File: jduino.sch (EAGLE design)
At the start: 21 parts, among them IC1 LM2936Z-5.0, IC2 ATMEGA48/88/168-PU, J4 6V - 30V in, Q1 16 mHz

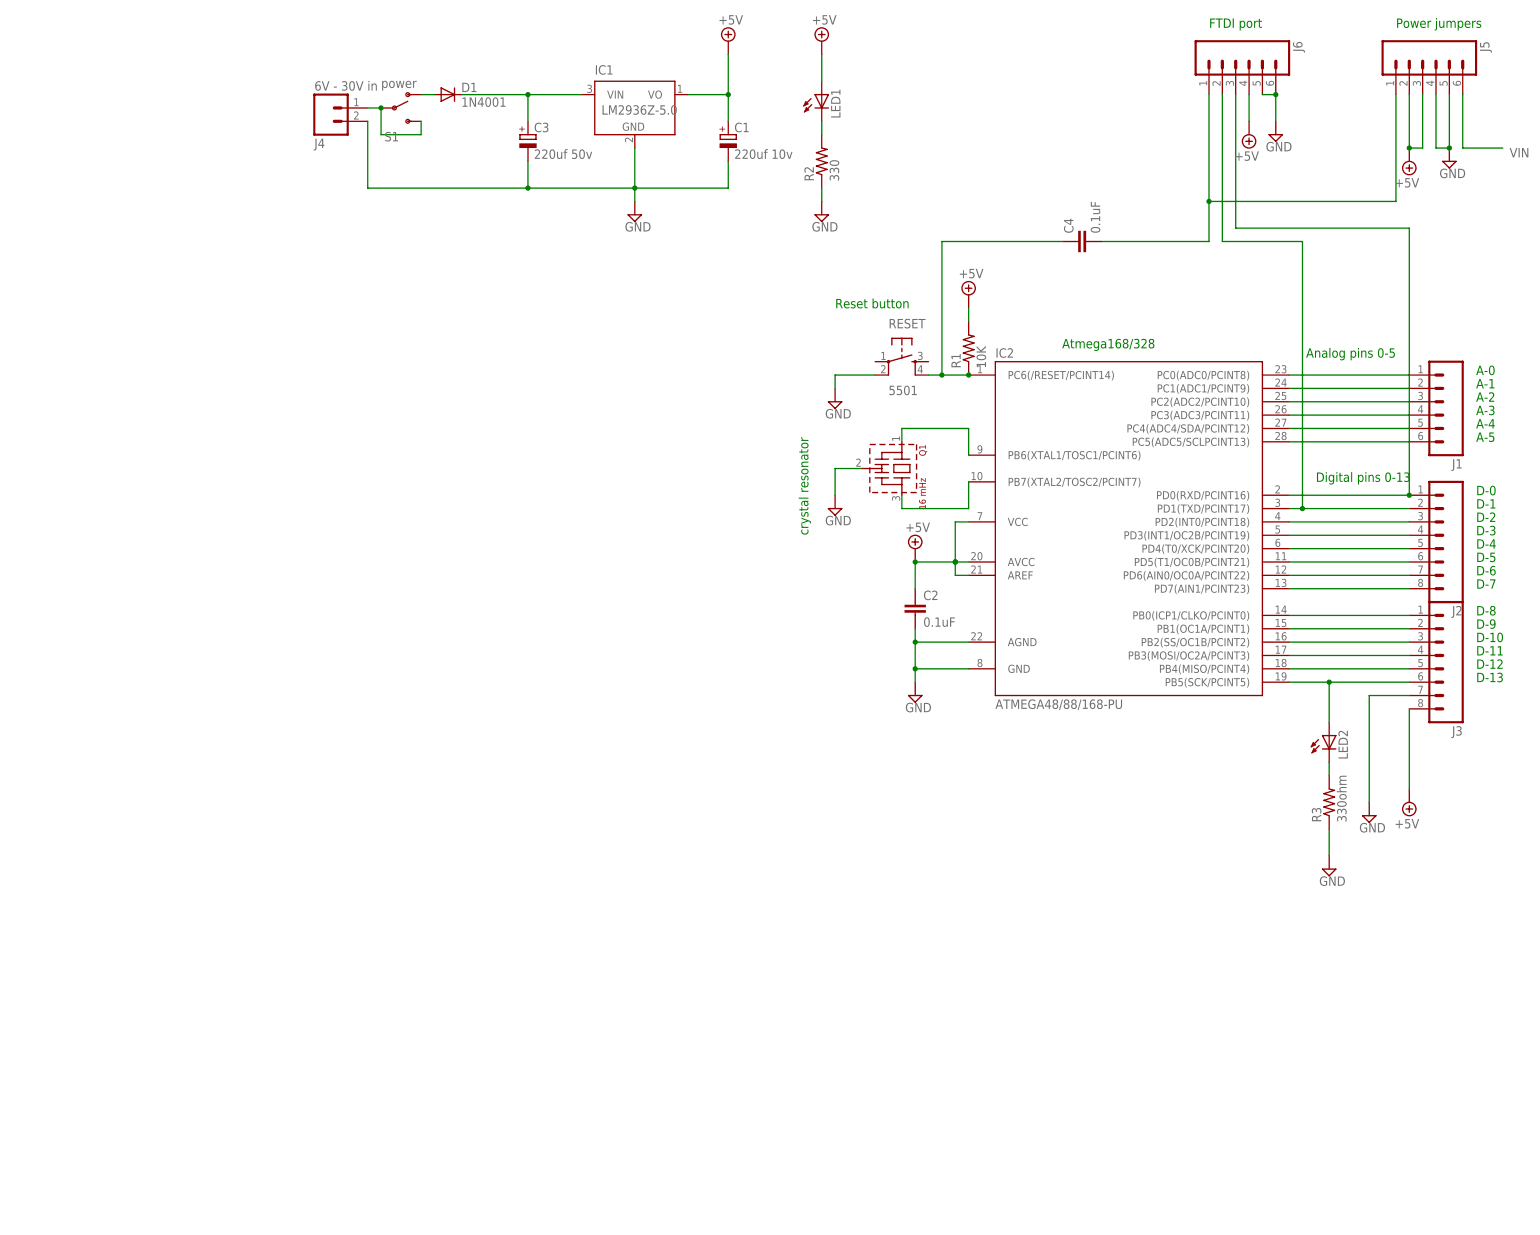
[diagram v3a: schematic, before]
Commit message: Reset adjustments and aesthetic improvements.
Connected reset pin on power jumper before DTR capacitor. Cleaned
up extraneous label and added a frame to the schematic.
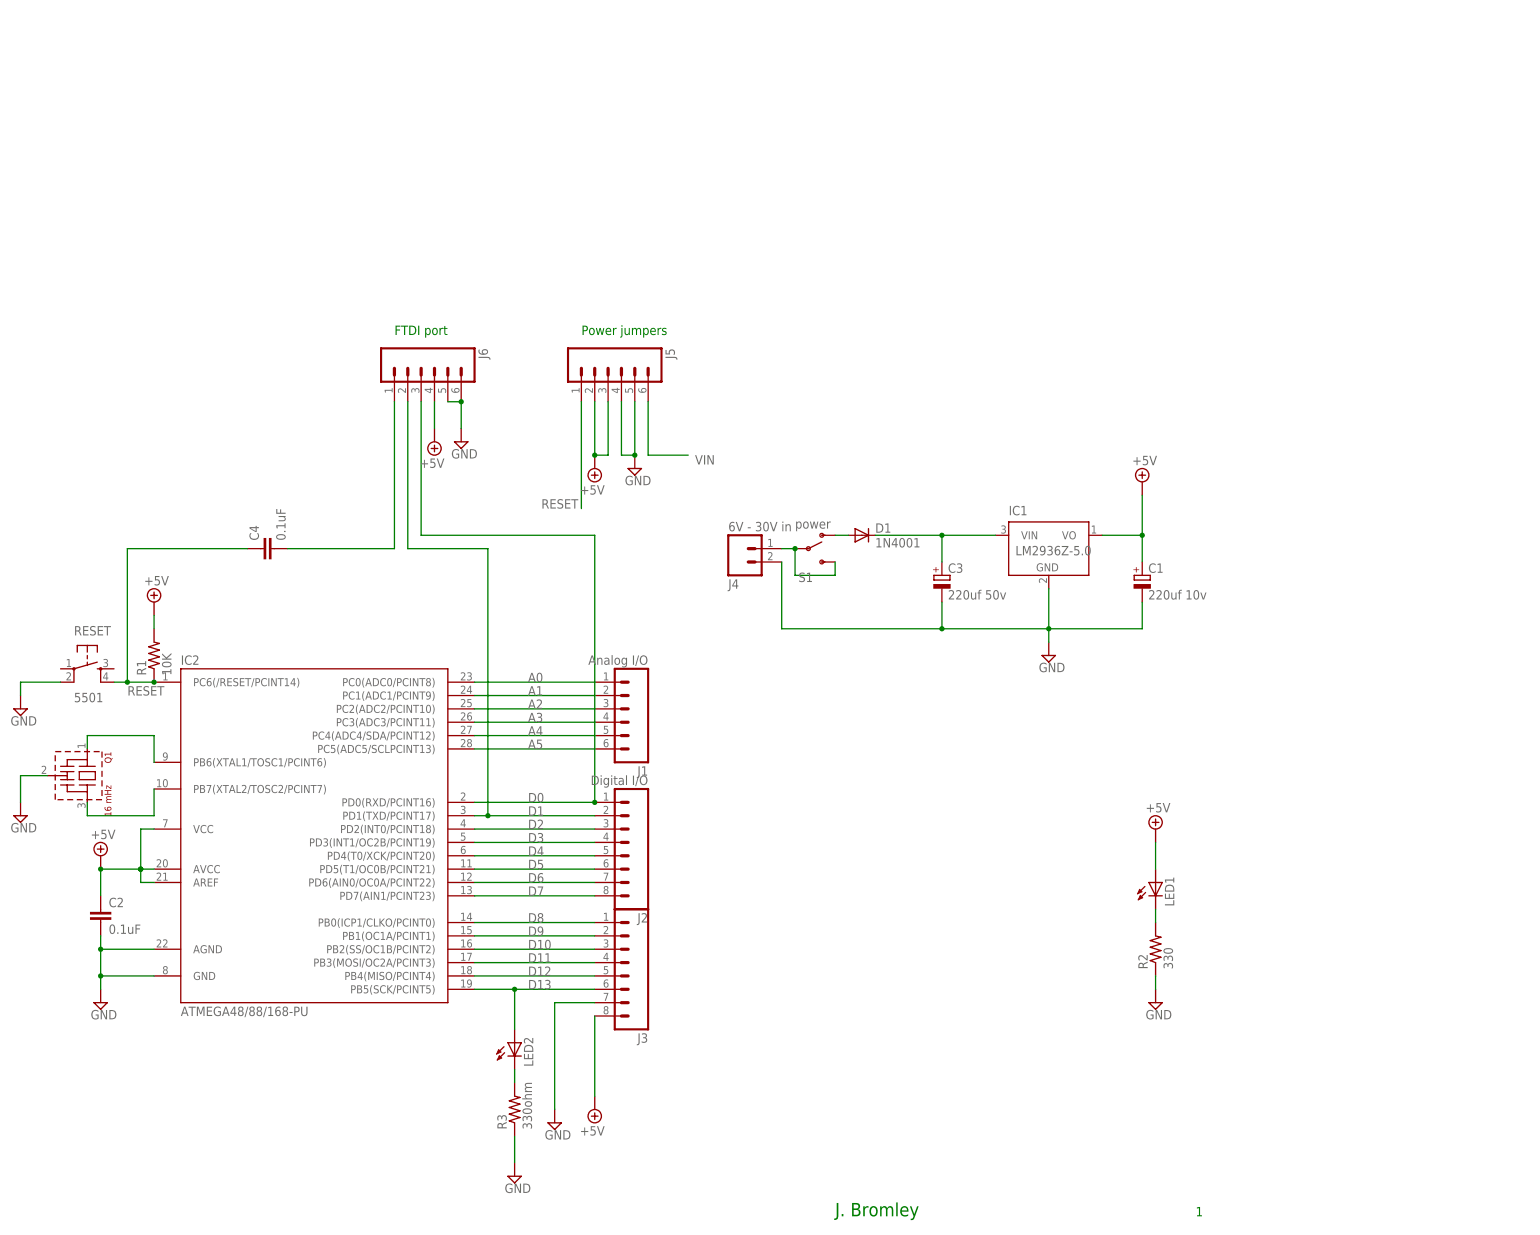
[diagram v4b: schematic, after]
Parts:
- J1: value (none) -> Analog I/O
- J2: value (none) -> Digital I/O
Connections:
- net N$1: no longer J5.1
- net RESET: now also J5.1
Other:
- note added: "1"
- note added: "J. Bromley"
- note removed: "A-0"
- note removed: "A-1"
- note removed: "A-2"
- note removed: "A-3"
- note removed: "A-4"
- note removed: "A-5"
- note removed: "Analog pins 0-5"
- note removed: "Atmega168/328"
- note removed: "D-0"
- note removed: "D-1"
- note removed: "D-10"
- note removed: "D-11"
- note removed: "D-12"
- note removed: "D-13"
- note removed: "D-2"
- note removed: "D-3"
- note removed: "D-4"
- note removed: "D-5"
- note removed: "D-6"
- note removed: "D-7"
- note removed: "D-8"
- note removed: "D-9"
- note removed: "Digital pins 0-13"
- note removed: "Reset button"
- note removed: "crystal resonator"
- moved on the sheet: C1, C2, C3, C4, D1, IC1, IC2, J1, J2, J3, J4, J5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

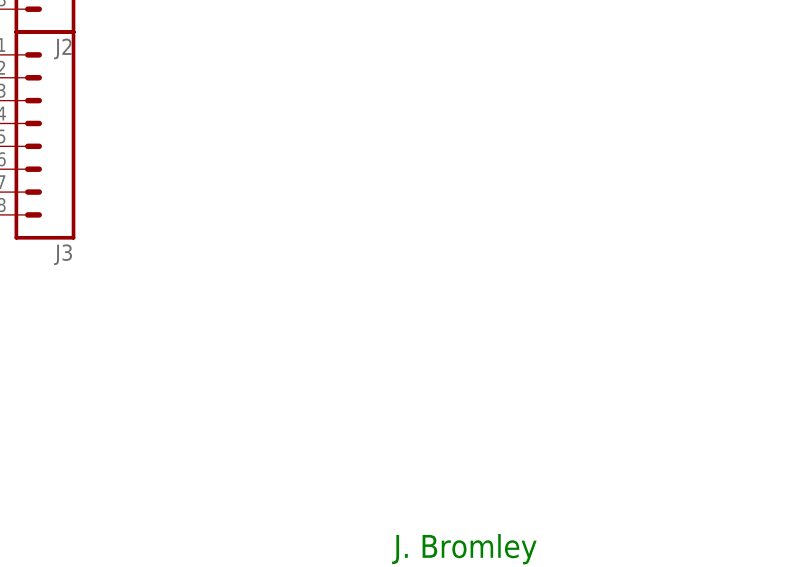
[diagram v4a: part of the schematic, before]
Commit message: Added mounting holes to the board.
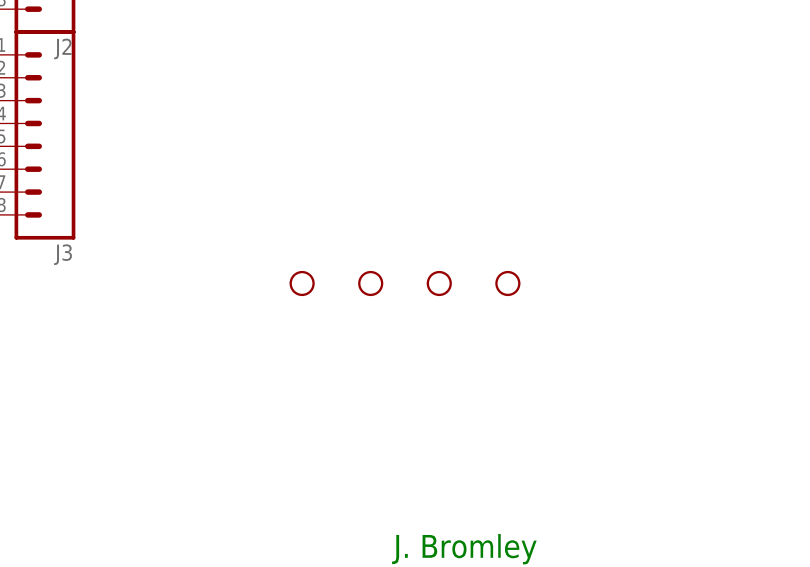
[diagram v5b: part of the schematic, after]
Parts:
- added JP1, JP2, JP3, JP4: STAND-OFF, SparkFun-Electromechanical:STAND-OFF
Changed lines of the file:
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@@
 <?xml version="1.0" encoding="utf-8"?>
 <!DOCTYPE eagle SYSTEM "eagle.dtd">
-<eagle version="6.1">
+<eagle version="6.2">
 <drawing>
 <settings>
@@
 <part name="C4" library="SparkFun-Passives" deviceset="CAP" device="PTH2" value="0.1uF"/>
 <part name="FRAME1" library="SparkFun-Aesthetics" deviceset="FRAME-LETTER" device=""/>
+<part name="JP1" library="SparkFun-Electromechanical" deviceset="STAND-OFF" device=""/>
+<part name="JP2" library="SparkFun-Electromechanical" deviceset="STAND-OFF" device=""/>
+<part name="JP3" library="SparkFun-Electromechanical" deviceset="STAND-OFF" device=""/>
+<part name="JP4" library="SparkFun-Electromechanical" deviceset="STAND-OFF" device=""/>
 </parts>
 <sheets>
@@
 <instance part="FRAME1" gate="G$1" x="-134.62" y="-91.44"/>
 <instance part="FRAME1" gate="G$2" x="12.7" y="-91.44"/>
+<instance part="JP1" gate="G$1" x="27.94" y="-53.34"/>
+<instance part="JP2" gate="G$1" x="35.56" y="-53.34"/>
+<instance part="JP3" gate="G$1" x="43.18" y="-53.34"/>
+<instance part="JP4" gate="G$1" x="50.8" y="-53.34"/>
 </instances>
 <busses>

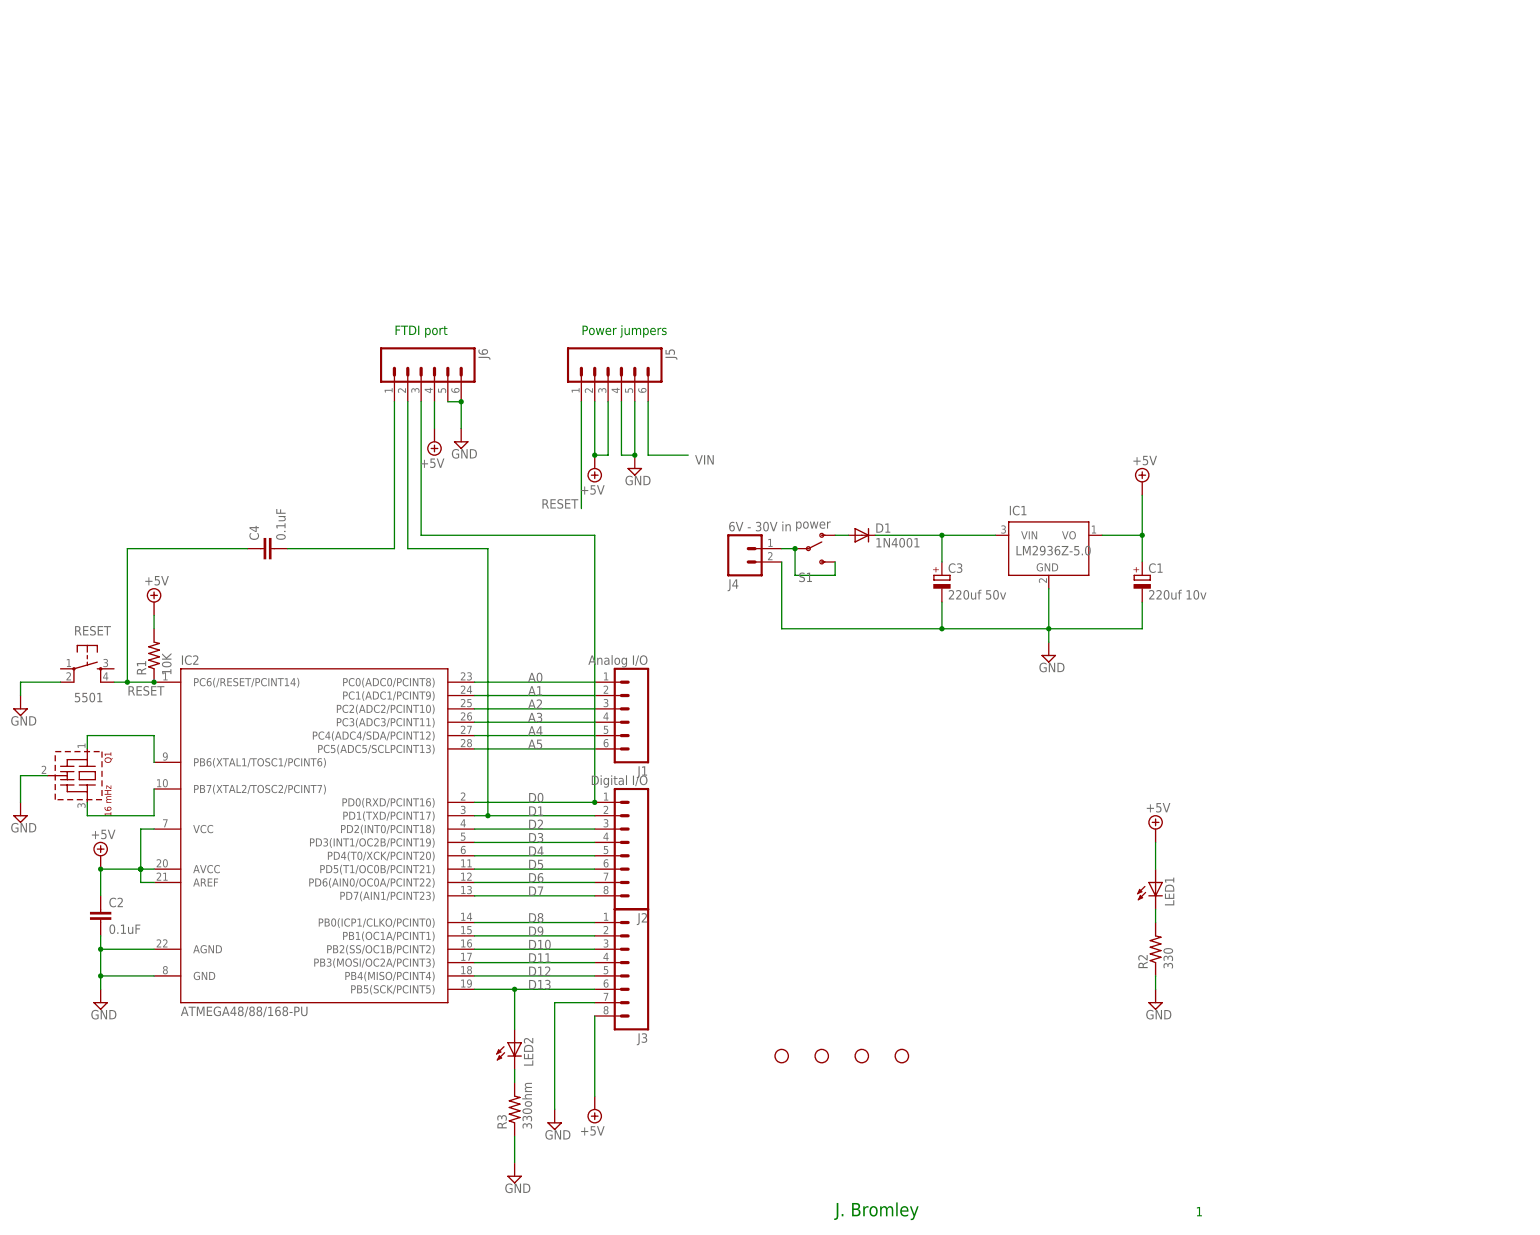
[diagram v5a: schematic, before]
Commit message: Completed layout.
Completed the board layout and sizing. Needed to include four top-side
jumpers.
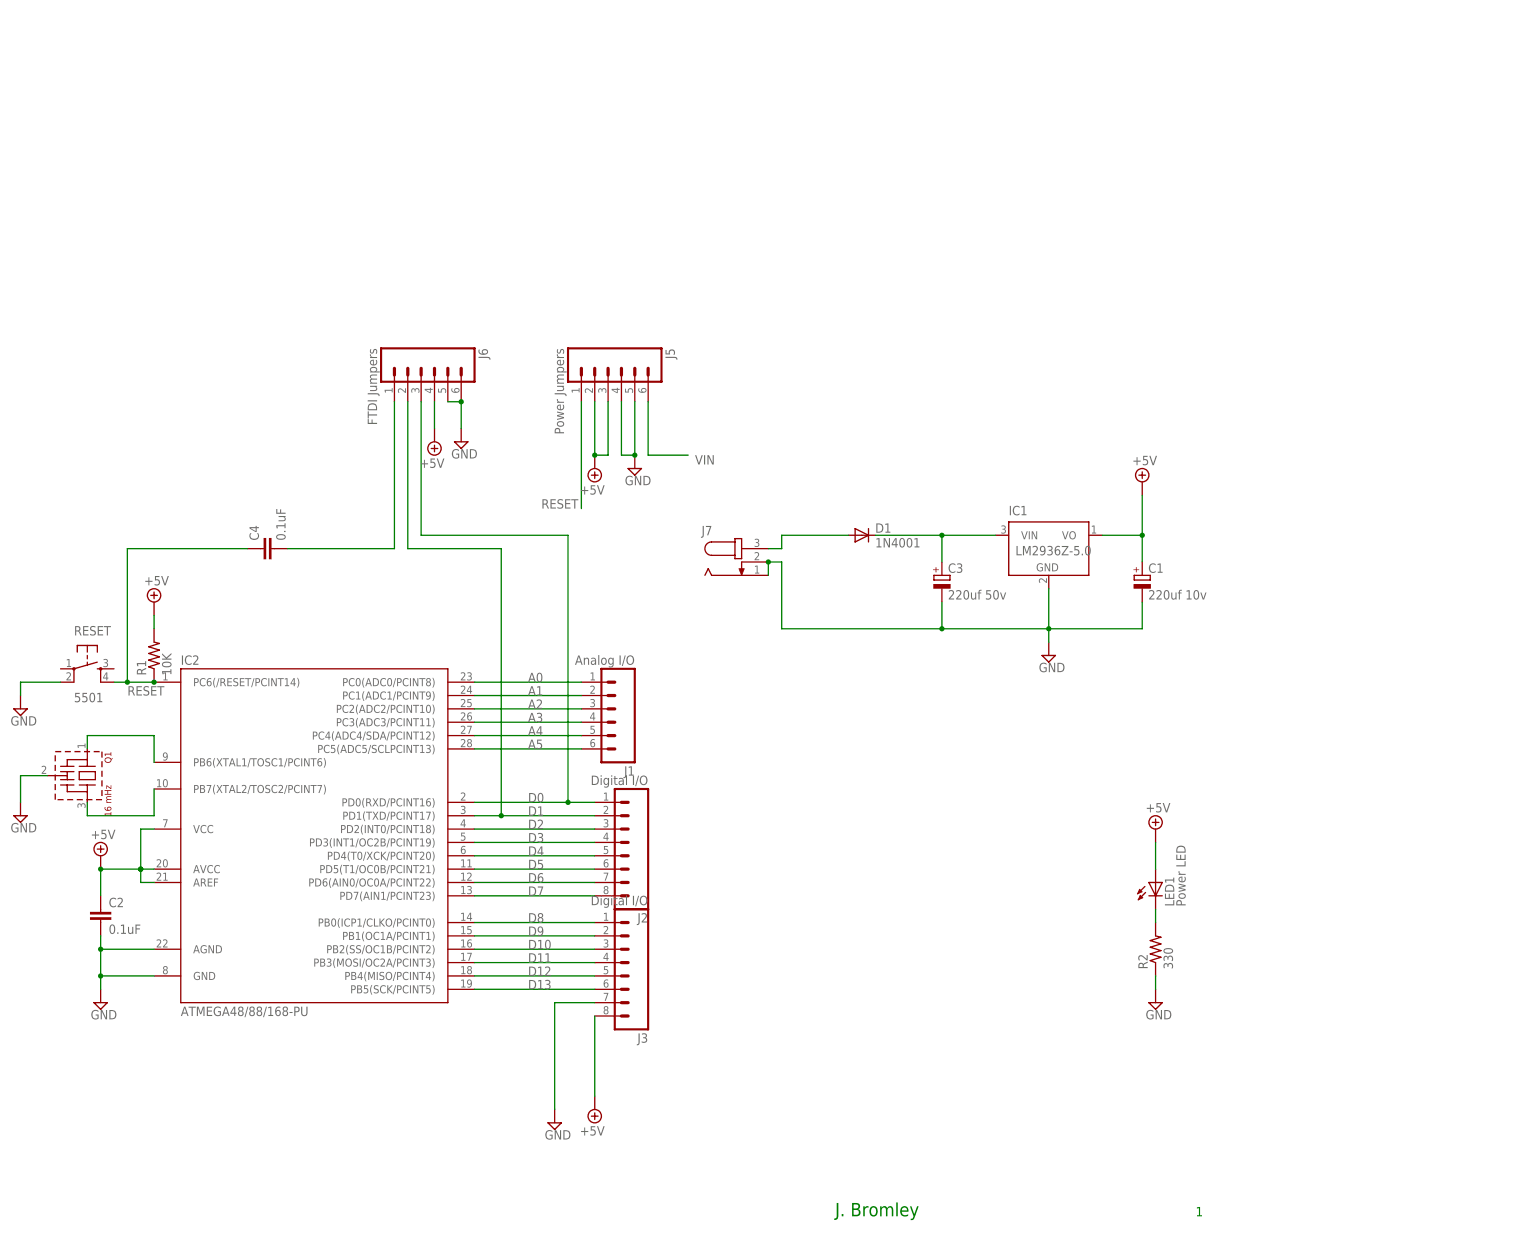
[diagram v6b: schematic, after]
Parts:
- removed J4: 6V - 30V in, SparkFun:M02LOCK
- removed JP1, JP2, JP3, JP4: STAND-OFF, SparkFun-Electromechanical:STAND-OFF
- removed LED2: (no value), led:LED3MM
- removed R3: 330ohm, rcl:R-US_0204/5
- removed S1: power, SparkFun-Electromechanical:SWITCH-SPDTPTH
- added J7: (no value), con-jack:JACK-PLUG1
- J3: value (none) -> Digital I/O
- J5: value (none) -> Power Jumpers
- J6: value (none) -> FTDI Jumpers
- LED1: value (none) -> Power LED
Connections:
- removed net N$4: LED2.C, R3.2
- removed net N$7: D1.A, S1.O
- net D13: no longer LED2.A
- net GND: now also J7.1, J7.2; no longer J4.2, R3.1
- net N$2: now also D1.A, J7.3; no longer J4.1, S1.P, S1.S
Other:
- note removed: "FTDI port"
- note removed: "Power jumpers"
- moved on the sheet: J1
